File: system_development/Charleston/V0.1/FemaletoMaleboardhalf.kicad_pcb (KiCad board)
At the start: 2 copper layers, 39 x 64.8 mm, 6 parts, among them J1 Screw_Terminal_01x12

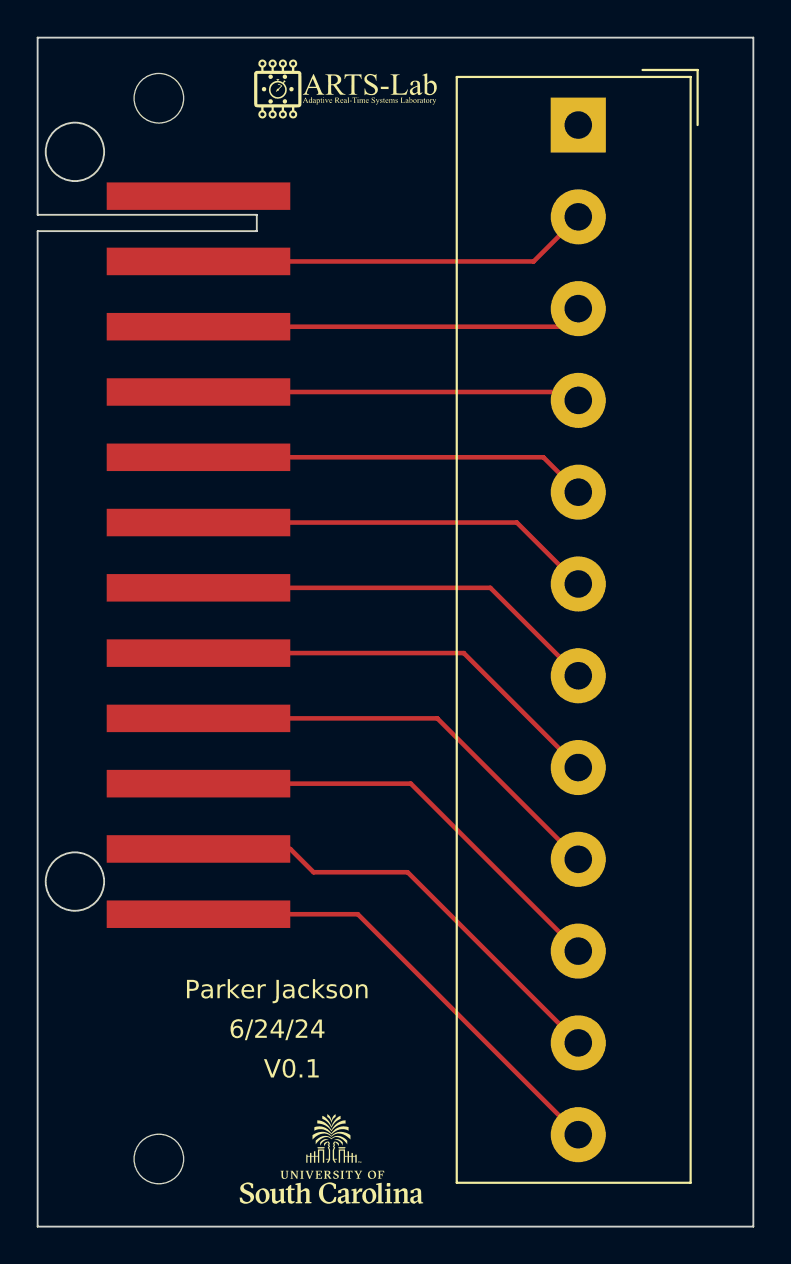
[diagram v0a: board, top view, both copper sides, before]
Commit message: Added Ground plane
and pushed it back to avoid electrocution
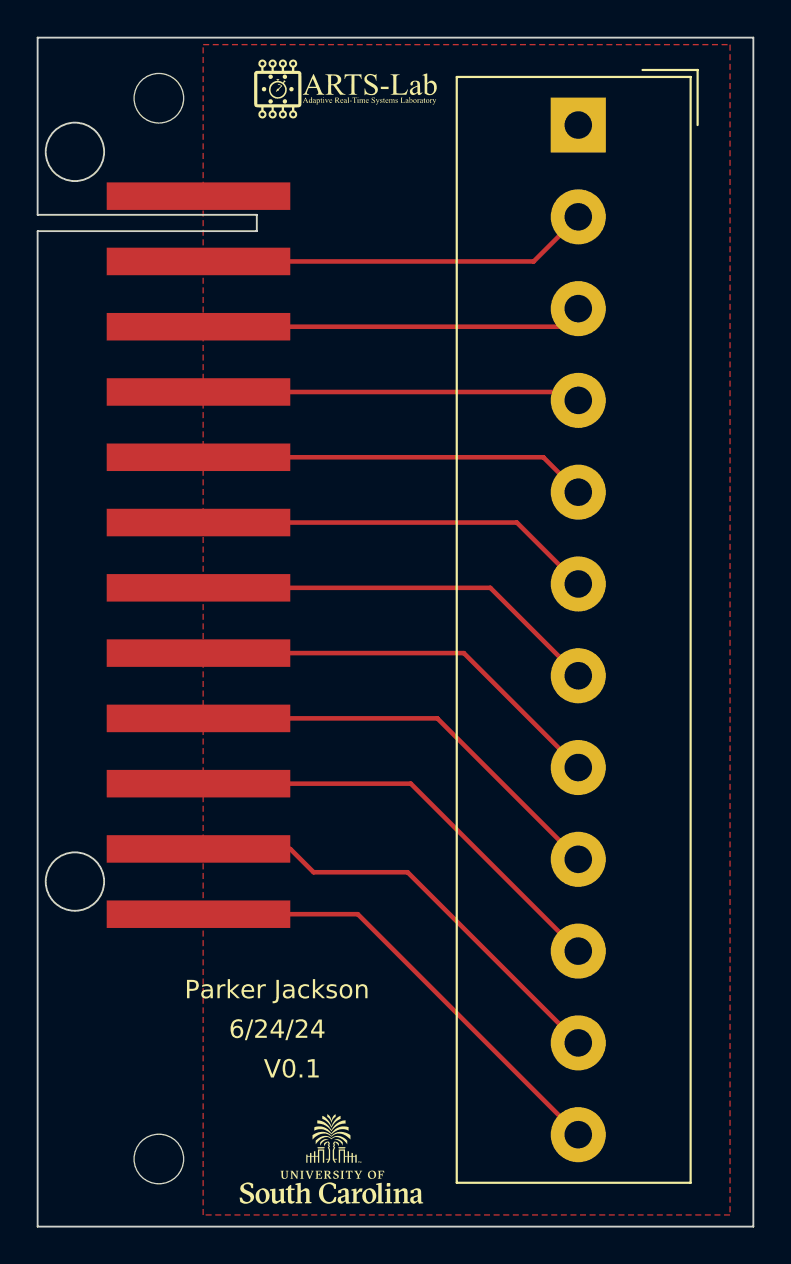
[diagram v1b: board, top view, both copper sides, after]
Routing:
- added copper zone on F.Cu, net GND
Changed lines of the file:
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@@
   (segment (start 119.38 90.043) (end 128.059 90.043) (width 0.25) (layer "F.Cu") (net 12))
   (segment (start 128.059 90.043) (end 140.069 102.053) (width 0.25) (layer "F.Cu") (net 12))
+  (zone (net 1) (net_name "GND") (layer "F.Cu") (hatch edge 0.5)
+    (connect_pads (clearance 0.5))
+    (min_thickness 0.25) (filled_areas_thickness no)
+    (fill yes (thermal_gap 0.5) (thermal_bridge_width 0.5))
+    (polygon
+      (pts
+        (xy 119.634 42.672)
+        (xy 148.336 42.672)
+        (xy 148.336 106.426)
+        (xy 119.634 106.426)
+      )
+    )
+  )
 )
